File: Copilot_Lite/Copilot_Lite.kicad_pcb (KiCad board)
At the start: 4 copper layers, 65 x 56 mm, 71 parts, among them J1 POWER_MODES, J11 SERIAL_MODE, J12 SERIAL_VOLTAGE_SELECT, J2 JACK_POWER_IN, J3 USB_POWER_IN, J4 USB_PC, J6 5V_ENABLE, J7 SERIAL_AND_GPIO, J8 JACK_POWER_OUT, J9 USB_POWER_OUT, Q1 BSS138, Q2 BUK7M27-80EX, Q3 BUK7M27-80EX, Q4 BSS138, Q5 BSS138, Q6 BSS138, Q7 BSS138, Q8 BSS138, U1 LM74502, U2 LM74502, U3 AP2204K-ADJ, U4 AP2204K-ADJ, U5 FT230XS, U6 TXB0104D

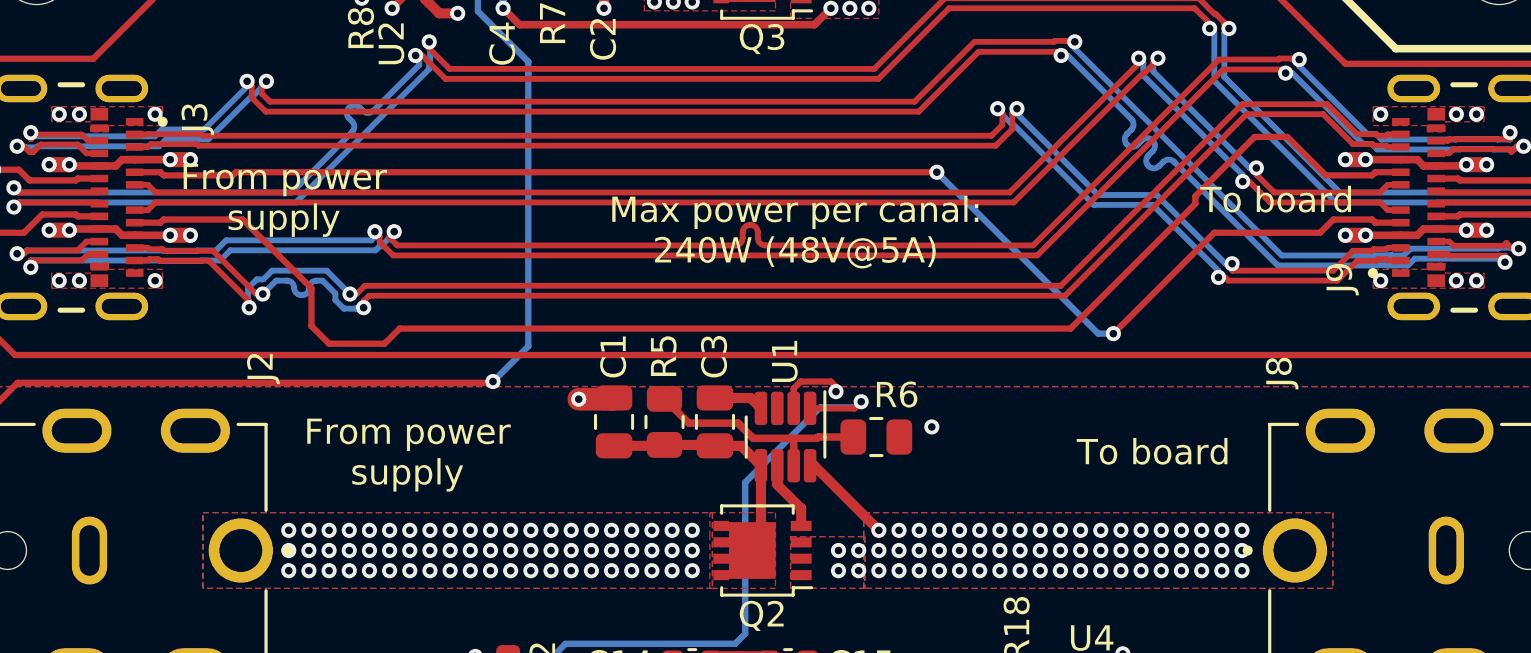
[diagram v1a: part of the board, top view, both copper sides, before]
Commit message: lite: Replaced 'From power supply' and 'To power supply' PCB texts by arrows, also fixed the maximum channel power PCB text.
Signed-off-by: Adrien Ricciardi <aricciardi@baylibre.com>
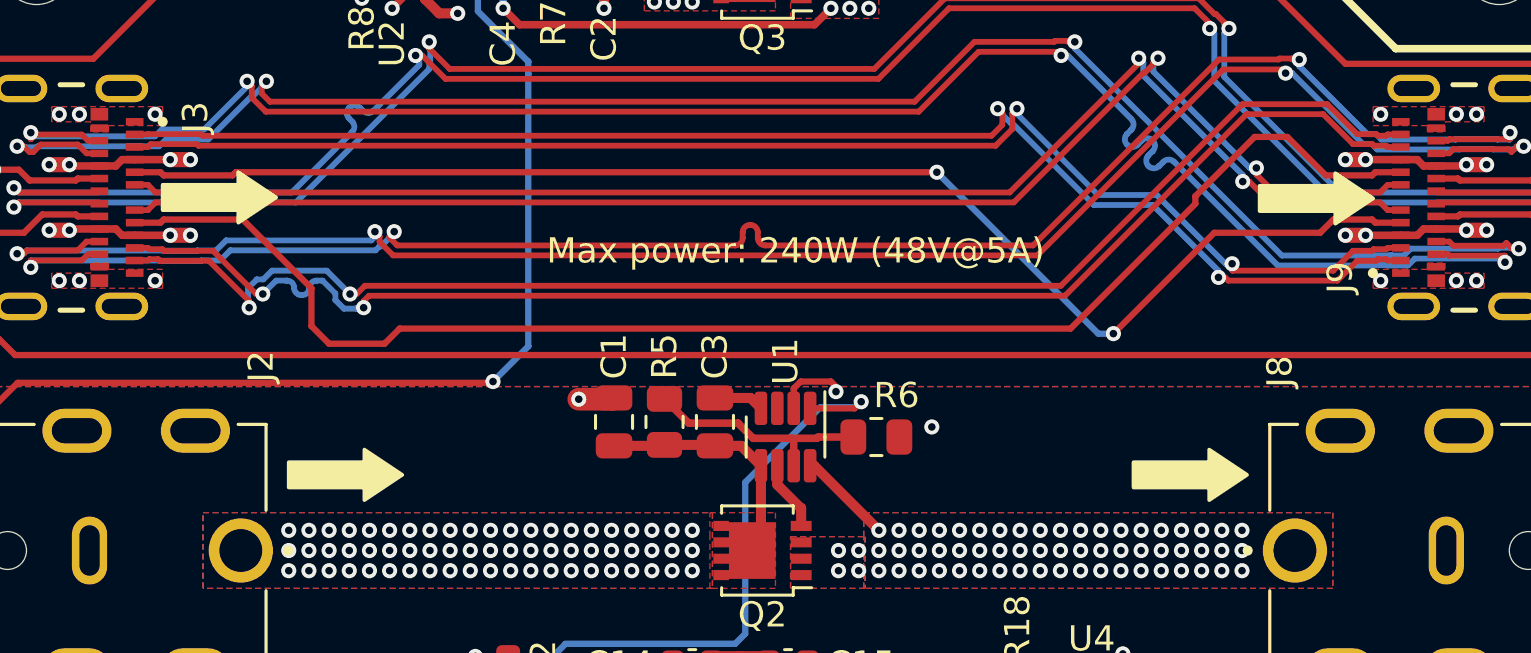
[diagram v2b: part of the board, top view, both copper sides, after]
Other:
- board text added: "Max power: 240W (48V@5A)"
- board text removed: "From power supply"
- board text removed: "Max power per canal: 240W (48V@5A)"
- board text removed: "To board"
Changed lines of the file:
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@@
   (gr_line (start 104 102.6) (end 104 100.2)
     (stroke (width 0.4) (type default)) (layer "B.SilkS"))
+  (gr_poly
+    (pts
+      (xy 76.5 68.5)
+      (xy 78 69.5)
+      (xy 76.5 70.5)
+    )
+    (stroke (width 0.15) (type solid)) (fill solid) (layer "F.SilkS"))
   (gr_line (start 122.4 63.6) (end 128.4 63.6)
     (stroke (width 0.3) (type default)) (layer "F.SilkS"))
+  (gr_poly
+    (pts
+      (xy 81.5 79.5)
+      (xy 83 80.5)
+      (xy 81.5 81.5)
+    )
+    (stroke (width 0.15) (type solid)) (fill solid) (layer "F.SilkS"))
+  (gr_poly
+    (pts
+      (xy 120 68.538462)
+      (xy 121.5 69.538462)
+      (xy 120 70.538462)
+    )
+    (stroke (width 0.15) (type solid)) (fill solid) (layer "F.SilkS"))
   (gr_line (start 119.7 60.9) (end 122.4 63.6)
     (stroke (width 0.3) (type default)) (layer "F.SilkS"))
+  (gr_rect (start 73.5 69) (end 76.5 70)
+    (stroke (width 0.15) (type solid)) (fill solid) (layer "F.SilkS"))
+  (gr_rect (start 117 69.038462) (end 120 70.038462)
+    (stroke (width 0.15) (type solid)) (fill solid) (layer "F.SilkS"))
   (gr_poly
     (pts
@@
       (xy 128.3 64.4)
     )
+    (stroke (width 0.15) (type solid)) (fill solid) (layer "F.SilkS"))
+  (gr_rect (start 78.5 80) (end 81.5 81)
+    (stroke (width 0.15) (type solid)) (fill solid) (layer "F.SilkS"))
+  (gr_poly
+    (pts
+      (xy 115 79.5)
+      (xy 116.5 80.5)
+      (xy 115 81.5)
+    )
+    (stroke (width 0.15) (type solid)) (fill solid) (layer "F.SilkS"))
+  (gr_rect (start 112 80) (end 115 81)
     (stroke (width 0.15) (type solid)) (fill solid) (layer "F.SilkS"))
   (gr_arc (start 130 110) (mid 129.12132 112.12132) (end 127 113)
@@
     (effects (font (size 1 1) (thickness 0.15)) (justify bottom))
   )
-  (gr_text "To board" (at 112.8 80.2) (layer "F.SilkS" knockout)
-    (effects (font (size 1 1) (thickness 0.15)) (justify bottom))
-  )
-  (gr_text "To board" (at 117.7 70.2) (layer "F.SilkS" knockout)
-    (effects (font (size 1 1) (thickness 0.15)) (justify bottom))
-  )
-  (gr_text "Max power per canal:\n240W (48V@5A)" (at 98.6 72.2) (layer "F.SilkS" knockout)
-    (effects (font (size 1 1) (thickness 0.15)) (justify bottom))
-  )
-  (gr_text "From power\nsupply" (at 83.2 81) (layer "F.SilkS" knockout)
+  (gr_text "Max power: 240W (48V@5A)" (at 98.6 72.2) (layer "F.SilkS" knockout)
     (effects (font (size 1 1) (thickness 0.15)) (justify bottom))
   )
@@
     (effects (font (size 1 1) (thickness 0.15)) (justify bottom))
   )
-  (gr_text "From power\nsupply" (at 78.3 70.9) (layer "F.SilkS" knockout)
-    (effects (font (size 1 1) (thickness 0.15)) (justify bottom))
-  )

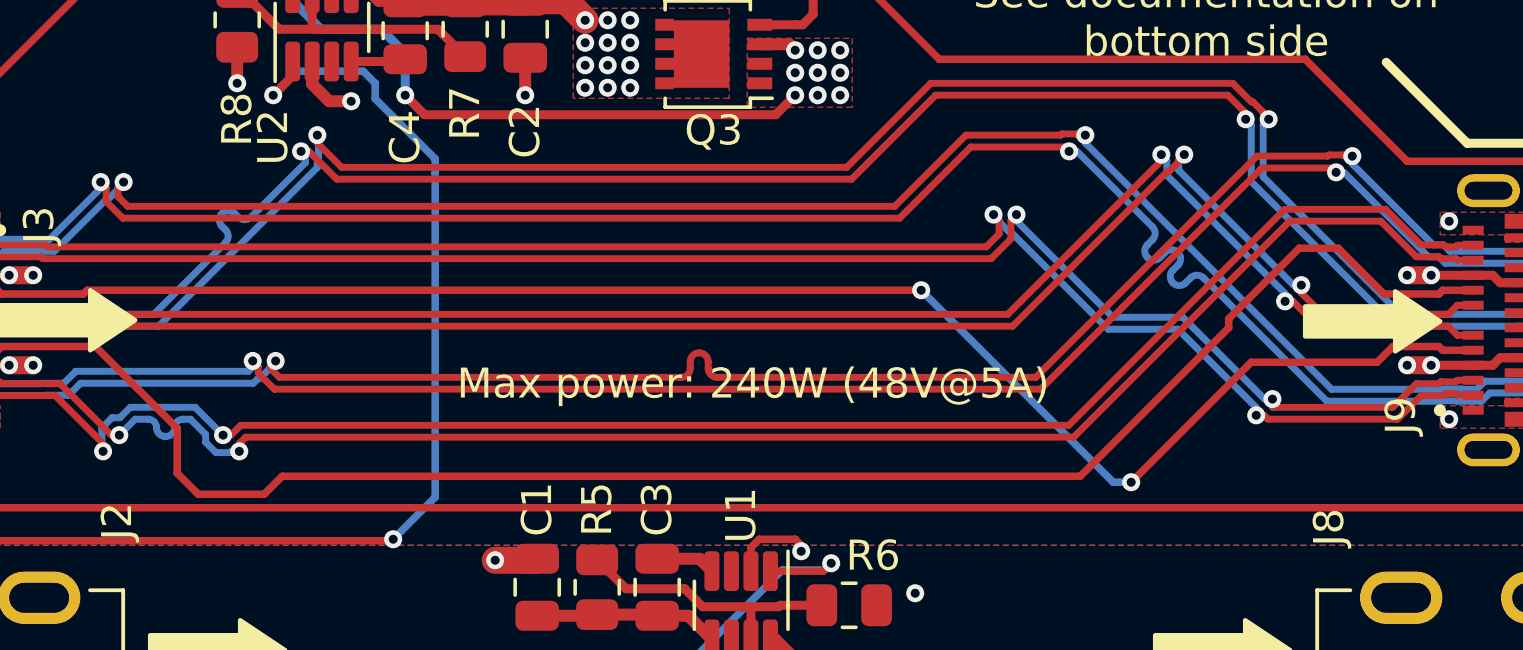
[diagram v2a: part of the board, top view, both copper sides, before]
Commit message: lite: Added BayLibre logo and board name and version to PCB.
Signed-off-by: Adrien Ricciardi <aricciardi@baylibre.com>
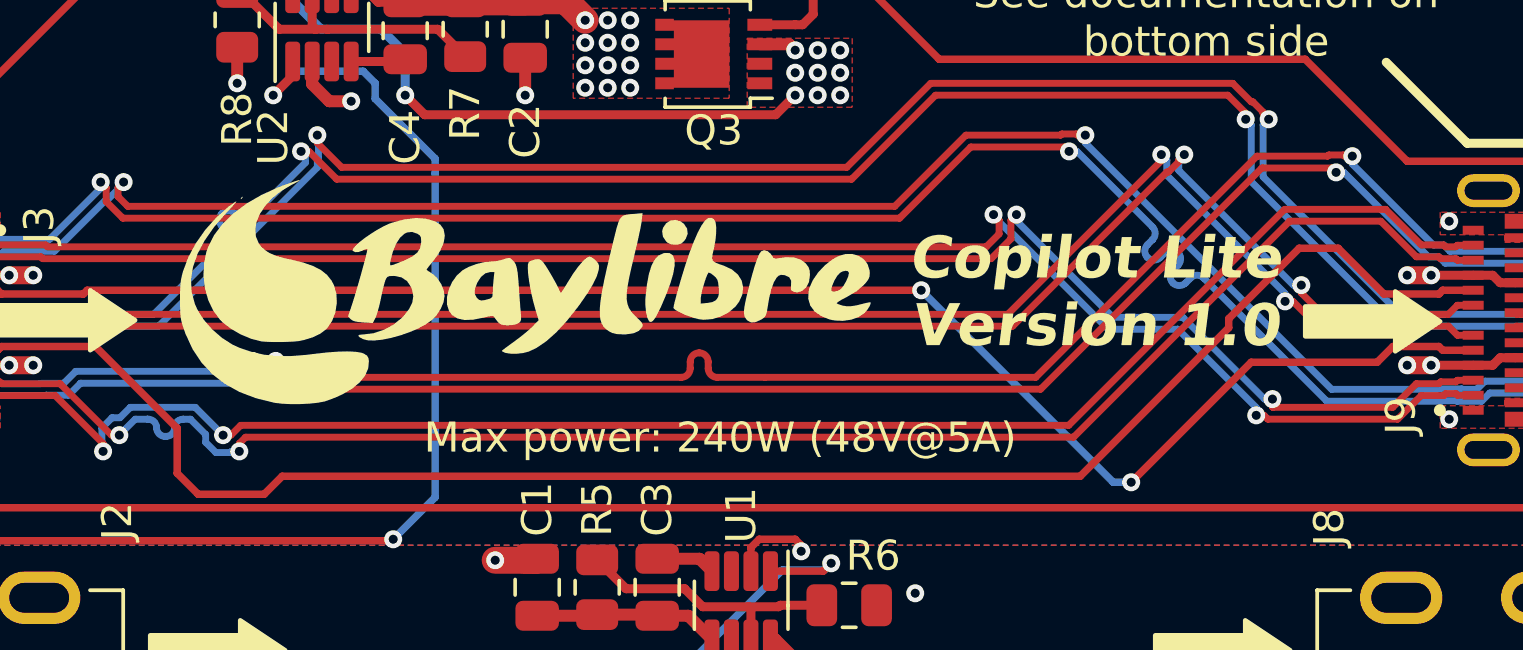
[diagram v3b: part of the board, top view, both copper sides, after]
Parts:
- added G***: LOGO, Logo_BayLibre:Logo_BayLibre, F.Cu at (91.0, 68.5)
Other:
- board text added: "Copilot Lite Version 1.0"

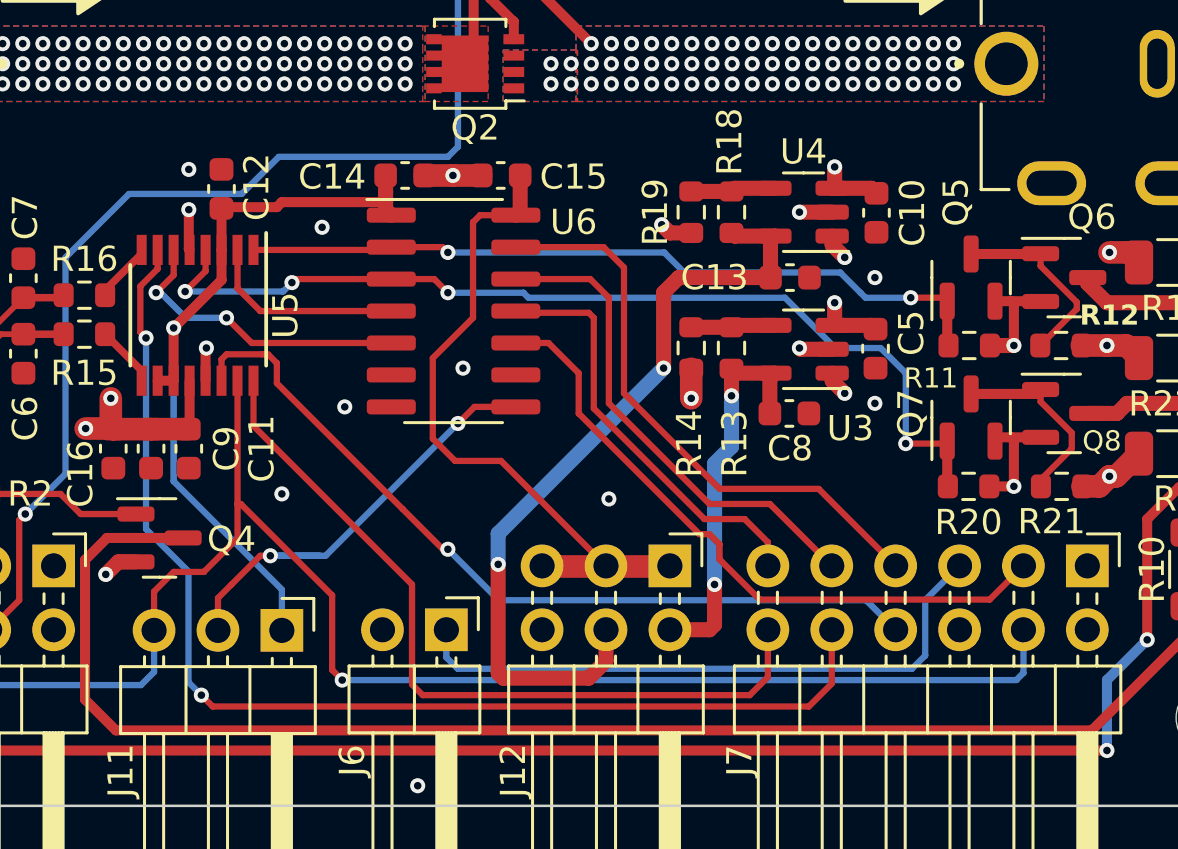
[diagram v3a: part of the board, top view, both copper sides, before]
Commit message: lite: Routed the new voltage translators. PCB silkscreen is not cleaned yet.
Signed-off-by: Adrien Ricciardi <aricciardi@baylibre.com>
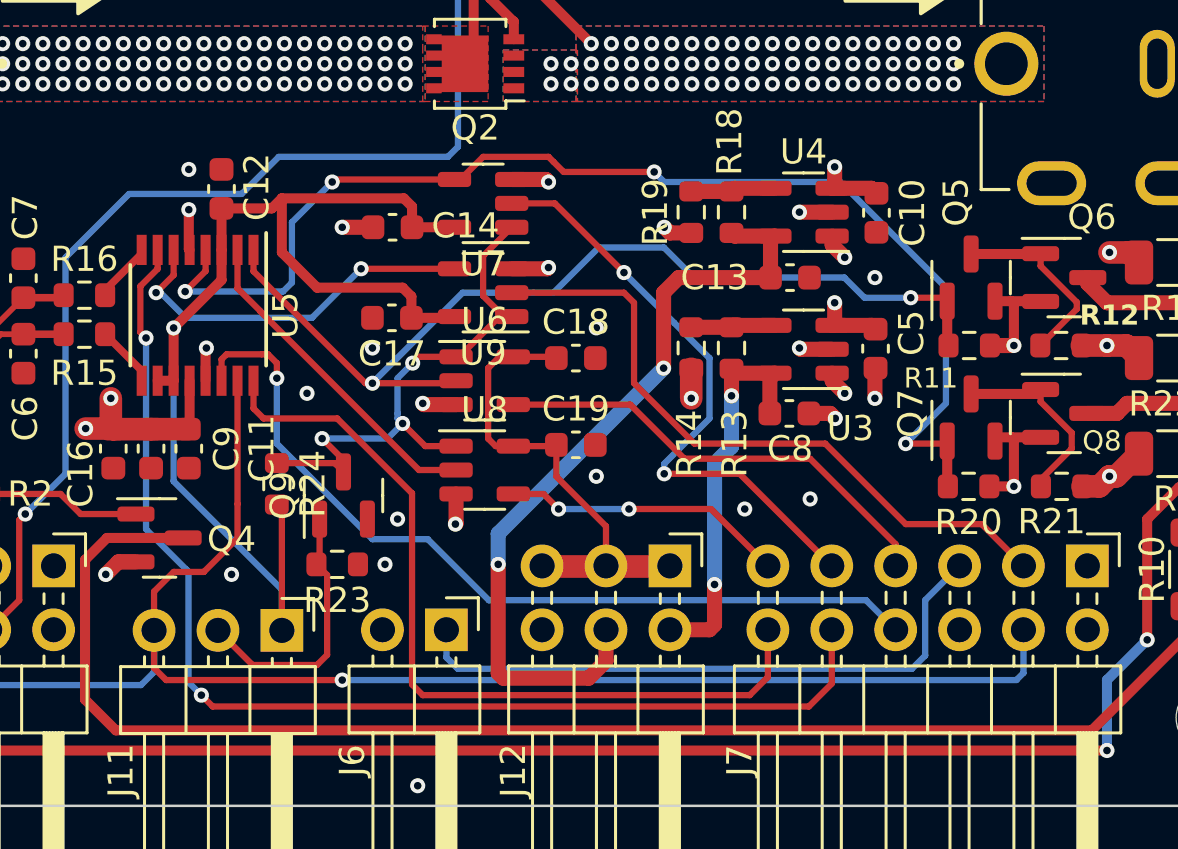
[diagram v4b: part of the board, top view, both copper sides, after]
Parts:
- removed C15: 100n, Capacitor_SMD:C_0603_1608Metric
- added C17: 100n, Capacitor_SMD:C_0603_1608Metric, F.Cu at (94.0, 93.6)
- added C18: 100n, Capacitor_SMD:C_0603_1608Metric, F.Cu at (101.3, 95.2)
- added C19: 100n, Capacitor_SMD:C_0603_1608Metric, F.Cu at (101.3, 98.7)
- added Q9: BSS138, Package_TO_SOT_SMD:SOT-23, F.Cu at (92.0, 100.7)
- added R23: 100K, Resistor_SMD:R_0603_1608Metric, F.Cu at (91.8, 103.4)
- added R24: 10K, Resistor_SMD:R_0603_1608Metric, F.Cu at (89.4, 100.2)
- added U7: SN74LV1T125, Package_TO_SOT_SMD:SOT-23-5, F.Cu at (97.6, 89.0)
- added U8: SN74LV1T125, Package_TO_SOT_SMD:SOT-23-5, F.Cu at (97.7, 99.7)
- added U9: SN74LV1T125, Package_TO_SOT_SMD:SOT-23-5, F.Cu at (97.6, 92.6)
- U6: value TXB0104D -> SN74LV1T125; footprint Package_SO:SOIC-14_3.9x8.7mm_P1.27mm -> Package_TO_SOT_SMD:SOT-23-5
- moved U6 3.03 mm to (97.7, 96.1)
- moved C14 2.12 mm to (94.0, 90.0), turned to 180 degrees
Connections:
- J12 pad 1: Net-(J12-Pin_1) -> /Controller/SERIAL_VOLTAGE
- J12 pad 3: Net-(J12-Pin_1) -> /Controller/SERIAL_VOLTAGE
- J12 pad 5: Net-(J12-Pin_1) -> /Controller/SERIAL_VOLTAGE
- U6 pad 1: +3.3VA -> /Controller//ENABLE
- U6 pad 3: /Controller/UART_RX -> GND
- U6 pad 4: Net-(U5-~{RTS}) -> /Controller/SERIAL_TX
- U6 pad 5: Net-(U5-~{CTS}) -> /Controller/SERIAL_VOLTAGE
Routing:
- net Net-(J12-Pin_1): track 26.8 -> 0.00 mm
- net /Controller//ENABLE: track 0.00 -> 22.5 mm, vias 0 -> 3
- net /Controller/SERIAL_VOLTAGE: track 0.00 -> 19.3 mm
- net +3.3VA: track 30.4 -> 48.2 mm
- net /Controller/UART_RX: track 38.7 -> 48.4 mm
- net /Controller/UART_TX: track 30.3 -> 38.6 mm
- net Net-(J11-Pin_2): track 18.3 -> 10.7 mm, vias 2 -> 0
- net GND: track 30.1 -> 36.8 mm, vias 50 -> 59
- net /Controller//SERIAL_RTS: track 16.9 -> 11.3 mm, vias 0 -> 2
- net Net-(U5-~{RTS}): track 8.01 -> 13.2 mm
- net /Controller/SERIAL_TX: track 23.3 -> 18.4 mm
- net /Controller/SERIAL_RX: track 19.7 -> 23.9 mm, vias 0 -> 2
- net Net-(U5-~{CTS}): track 12.2 -> 15.1 mm
- net /Controller/GPIO_3: track 31.2 -> 32.9 mm
- net /Controller/GPIO_1: track 32.7 -> 34.1 mm
